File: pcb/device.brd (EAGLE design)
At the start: 160 x 100 mm, 19 parts, among them IC1 TINY13-20PU

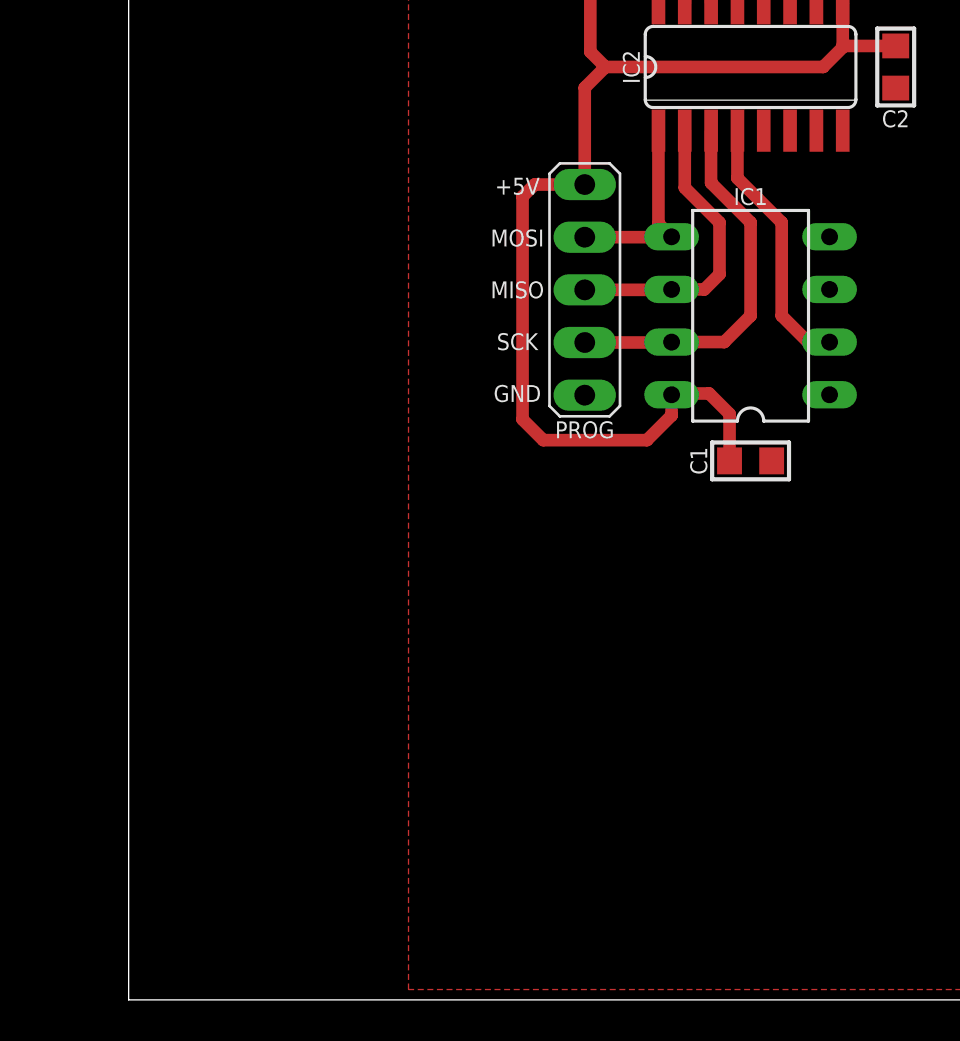
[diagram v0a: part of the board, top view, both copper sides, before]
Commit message: Fix motor connection and add pullup on action pin.
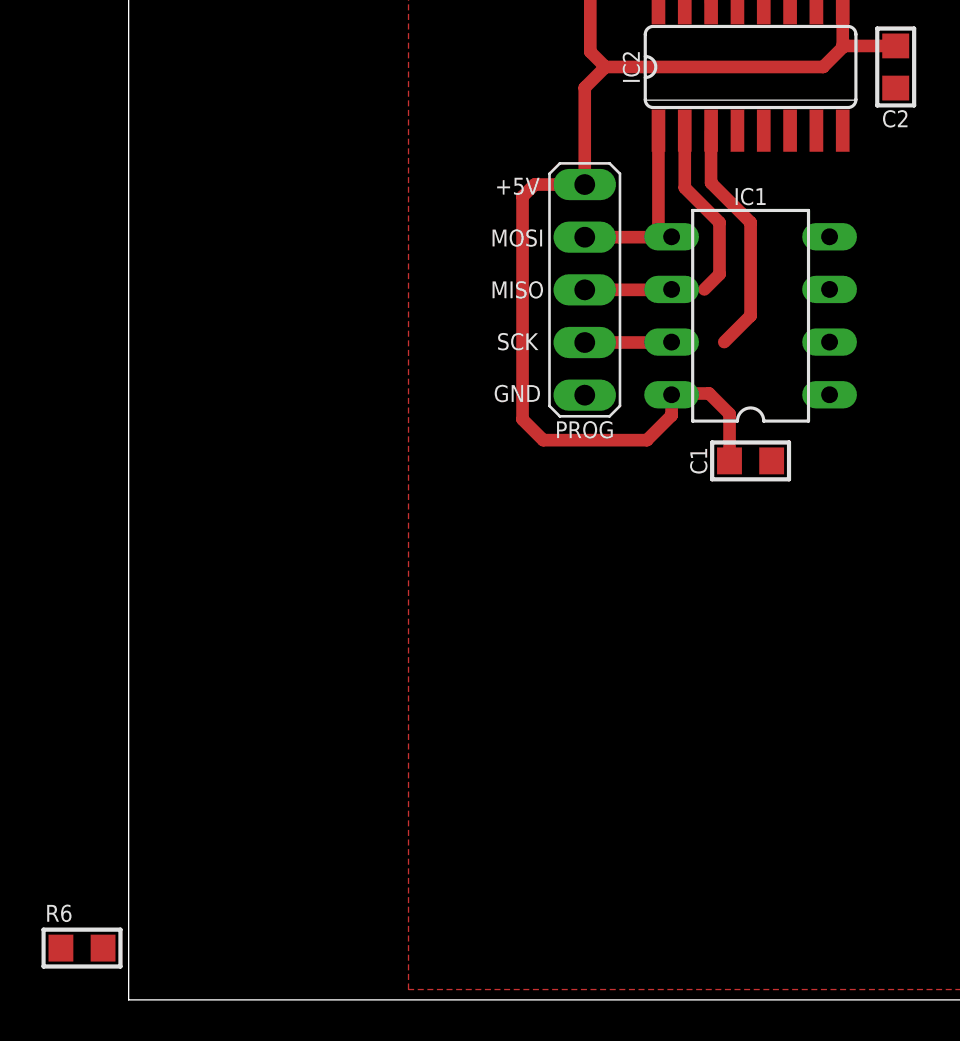
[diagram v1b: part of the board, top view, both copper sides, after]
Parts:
- added R6: 10k, rc-master-smd:R0805
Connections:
- net N$18 renamed !RESET
- removed net N$17: ACTION.1, IC1.3
- new net ROTATE: ACTION.1, IC1.3, R6.1
- net +5V: now also R6.2
- net MISO: now also IC1.7; no longer IC1.6
- net MOSI: now also IC1.6; no longer IC1.5
- net SCK: now also IC1.5; no longer IC1.7
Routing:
- net N$6: track 12.6 -> 0.00 mm
- net SCK: track 18.3 -> 15.7 mm
- net MISO: track 14.4 -> 12.8 mm
- net MOSI: track 9.58 -> 8.65 mm
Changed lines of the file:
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@@
 <attribute name="NAME" x="18.48" y="58.972" size="0.8128" layer="25" font="vector" ratio="18" rot="R90" align="center"/>
 </element>
+<element name="R6" library="rc-master-smd" package="R0805" value="10k" x="-2.25" y="2.5"/>
 </elements>
 <signals>
@@
 <wire x1="22.27" y1="56" x2="22.27" y2="58.746" width="0.6096" layer="1"/>
 <wire x1="22.27" y1="58.746" x2="22.016" y2="59" width="0.6096" layer="1"/>
+<contactref element="R6" pad="2"/>
+<wire x1="-1.234" y1="2.5" x2="20" y2="27" width="0" layer="19" extent="1-1"/>
 </signal>
 <signal name="N$1">
@@
 </signal>
 <signal name="MOSI">
-<contactref element="IC1" pad="5"/>
 <contactref element="IC2" pad="1"/>
 <contactref element="PROG" pad="2"/>
 <wire x1="22" y1="36.79" x2="26.17" y2="36.79" width="0.6096" layer="1"/>
-<wire x1="26.17" y1="36.79" x2="26.19" y2="36.81" width="0.6096" layer="1"/>
 <wire x1="25.555" y1="41.9266" x2="25.555" y2="37.445" width="0.6096" layer="1"/>
-<wire x1="25.555" y1="37.445" x2="26.19" y2="36.81" width="0.6096" layer="1"/>
+<contactref element="IC1" pad="6"/>
+<wire x1="26.17" y1="36.79" x2="25.555" y2="37.445" width="0" layer="19" extent="1-1"/>
+<wire x1="26.19" y1="34.27" x2="26.17" y2="36.79" width="0" layer="19" extent="1-1"/>
 </signal>
 <signal name="MISO">
-<contactref element="IC1" pad="6"/>
 <contactref element="IC2" pad="2"/>
 <contactref element="PROG" pad="3"/>
 <wire x1="22" y1="34.25" x2="26.17" y2="34.25" width="0.6096" layer="1"/>
-<wire x1="26.17" y1="34.25" x2="26.19" y2="34.27" width="0.6096" layer="1"/>
 <wire x1="26.825" y1="41.9266" x2="26.825" y2="39.175" width="0.6096" layer="1"/>
 <wire x1="26.825" y1="39.175" x2="28.5" y2="37.5" width="0.6096" layer="1"/>
-<wire x1="26.19" y1="34.27" x2="27.77" y2="34.27" width="0.6096" layer="1"/>
 <wire x1="27.77" y1="34.27" x2="28.5" y2="35" width="0.6096" layer="1"/>
 <wire x1="28.5" y1="35" x2="28.5" y2="37.5" width="0.6096" layer="1"/>
+<contactref element="IC1" pad="7"/>
+<wire x1="26.17" y1="34.25" x2="27.77" y2="34.27" width="0" layer="19" extent="1-1"/>
+<wire x1="26.19" y1="31.73" x2="26.17" y2="34.25" width="0" layer="19" extent="1-1"/>
 </signal>
 <signal name="SCK">
-<contactref element="IC1" pad="7"/>
 <contactref element="IC2" pad="3"/>
 <contactref element="PROG" pad="4"/>
 <wire x1="28.095" y1="41.9266" x2="28.095" y2="39.405" width="0.6096" layer="1"/>
 <wire x1="28.095" y1="39.405" x2="30" y2="37.5" width="0.6096" layer="1"/>
-<wire x1="26.19" y1="31.73" x2="28.73" y2="31.73" width="0.6096" layer="1"/>
 <wire x1="28.73" y1="31.73" x2="30" y2="33" width="0.6096" layer="1"/>
 <wire x1="30" y1="33" x2="30" y2="37.5" width="0.6096" layer="1"/>
 <wire x1="22" y1="31.71" x2="26.17" y2="31.71" width="0.6096" layer="1"/>
-<wire x1="26.17" y1="31.71" x2="26.19" y2="31.73" width="0.6096" layer="1"/>
-</signal>
-<signal name="N$8">
-<contactref element="IC1" pad="2"/>
-<contactref element="IC2" pad="4"/>
-<wire x1="29.365" y1="41.9266" x2="29.365" y2="39.635" width="0.6096" layer="1"/>
-<wire x1="29.365" y1="39.635" x2="31.5" y2="37.5" width="0.6096" layer="1"/>
-<wire x1="33.81" y1="31.73" x2="32.77" y2="31.73" width="0.6096" layer="1"/>
-<wire x1="32.77" y1="31.73" x2="31.5" y2="33" width="0.6096" layer="1"/>
-<wire x1="31.5" y1="33" x2="31.5" y2="37.5" width="0.6096" layer="1"/>
+<contactref element="IC1" pad="5"/>
+<wire x1="28.095" y1="39.405" x2="26.19" y2="36.81" width="0" layer="19" extent="1-1"/>
+<wire x1="26.17" y1="31.71" x2="28.73" y2="31.73" width="0" layer="19" extent="1-1"/>
 </signal>
 <signal name="BLUE">
@@
 <wire x1="32.54" y1="56" x2="32.54" y2="55.54" width="0.6096" layer="1"/>
 </signal>
-<signal name="N$17">
-<contactref element="IC1" pad="3"/>
-<contactref element="ACTION" pad="1"/>
-<wire x1="43.66" y1="10.79" x2="33.81" y2="34.27" width="0" layer="19" extent="1-1"/>
-</signal>
-<signal name="N$18">
-<contactref element="IC1" pad="1"/>
-<contactref element="MODE" pad="1"/>
-<wire x1="33.81" y1="29.19" x2="43.97" y2="23.96" width="0" layer="19" extent="1-1"/>
-</signal>
 <signal name="N$5">
 <contactref element="R5" pad="1"/>
@@
 <wire x1="19.984" y1="60.966" x2="19.95" y2="61" width="0.6096" layer="1"/>
 </signal>
+<signal name="N$6">
+<contactref element="IC1" pad="2"/>
+<contactref element="IC2" pad="4"/>
+<wire x1="33.81" y1="31.73" x2="29.365" y2="41.9266" width="0" layer="19" extent="1-1"/>
+</signal>
+<signal name="ROTATE">
+<contactref element="IC1" pad="3"/>
+<contactref element="ACTION" pad="1"/>
+<contactref element="R6" pad="1"/>
+<wire x1="43.66" y1="10.79" x2="33.81" y2="34.27" width="0" layer="19" extent="1-1"/>
+<wire x1="-3.266" y1="2.5" x2="43.66" y2="10.79" width="0" layer="19" extent="1-1"/>
+</signal>
+<signal name="!RESET">
+<contactref element="IC1" pad="1"/>
+<contactref element="MODE" pad="1"/>
+<wire x1="33.81" y1="29.19" x2="43.97" y2="23.96" width="0" layer="19" extent="1-1"/>
+</signal>
 </signals>

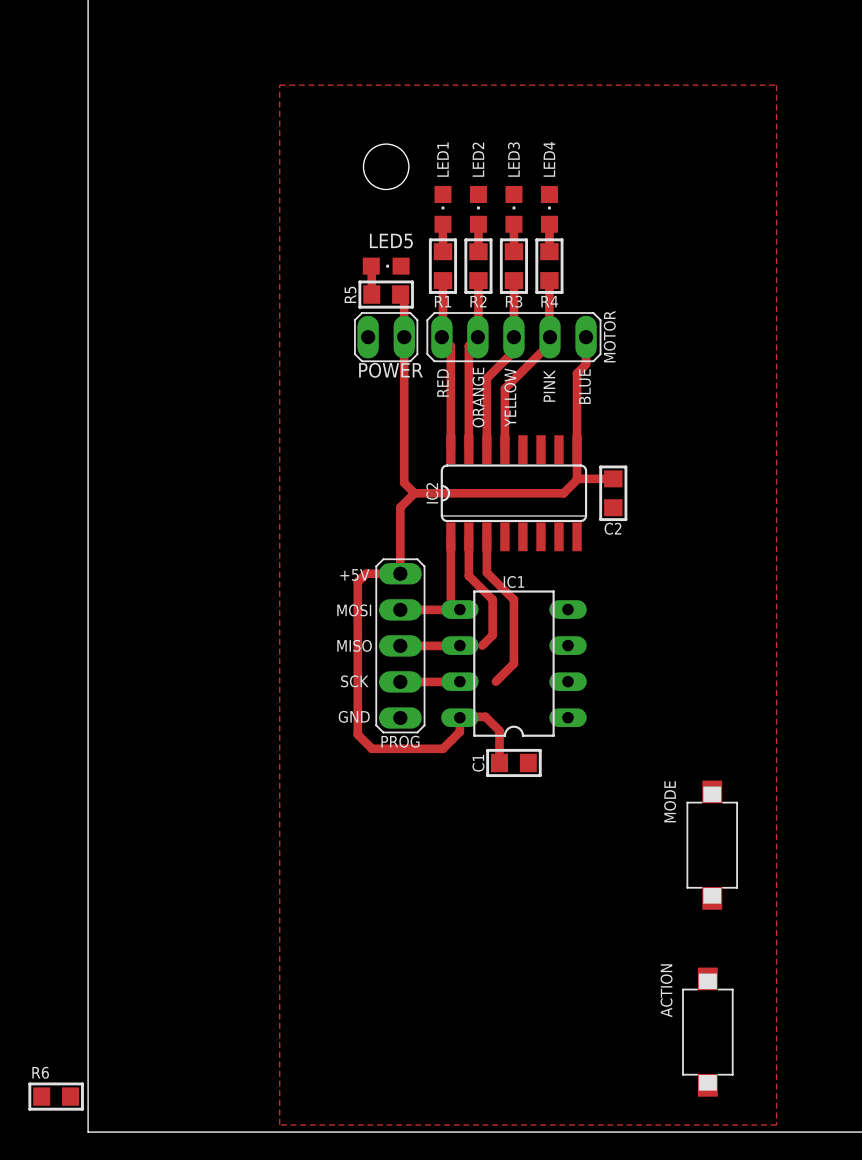
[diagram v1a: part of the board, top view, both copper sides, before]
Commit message: Almost ready PCB.
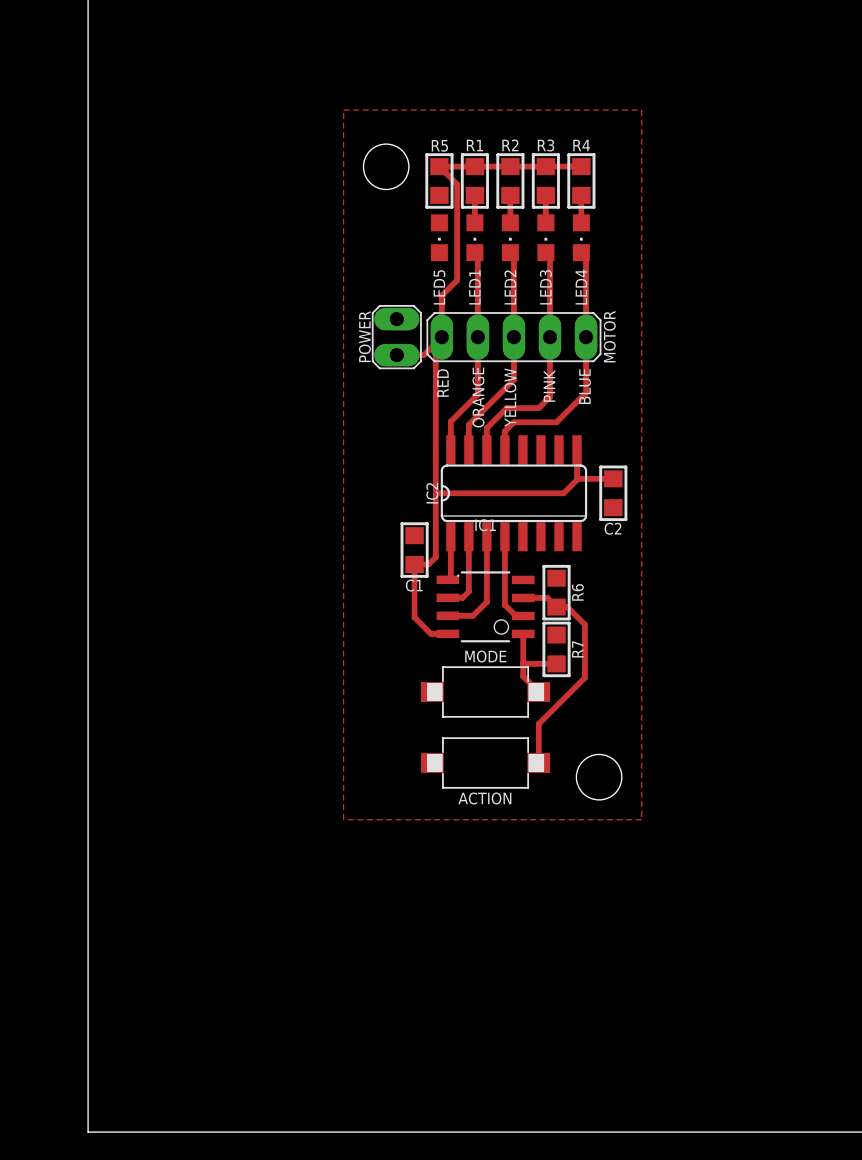
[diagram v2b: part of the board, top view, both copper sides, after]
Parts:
- removed PROG: (no value), pinhead-fixdrills:1X05
- added R7: 10k, rc-master-smd:R0805
- IC1: value TINY13-20PU -> TINY13-20SSU; device avr:DIL08 -> avr:8S1
- moved R6 50.0 mm to (33.0, 38.0), turned to 90 degrees
- moved ACTION 24.6 mm to (28.0, 26.0), turned to 180 degrees
- moved MODE 19.3 mm to (28.0, 31.0), turned to 180 degrees
- moved C1 16.6 mm to (23.0, 41.0), turned to 90 degrees
- moved R5 8.84 mm to (24.8, 67.0), turned to 90 degrees
- moved R1 6.41 mm to (27.2, 67.0), turned to 90 degrees
- moved R2 6.41 mm to (29.8, 67.0), turned to 90 degrees
- moved R3 6.41 mm to (32.2, 67.0), turned to 90 degrees
- moved R4 6.41 mm to (34.8, 67.0), turned to 90 degrees
- moved IC1 4.47 mm to (28.0, 37.0)
- moved LED5 4.25 mm to (24.8, 63.0), turned to 180 degrees
- moved LED1 3.01 mm to (27.2, 63.0), turned to 180 degrees
- moved LED2 3.01 mm to (29.8, 63.0), turned to 180 degrees
- moved LED3 3.01 mm to (32.2, 63.0), turned to 180 degrees
- moved LED4 3.01 mm to (34.8, 63.0), turned to 180 degrees
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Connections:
- removed net MISO: IC1.7, IC2.2, PROG.3
- removed net MOSI: IC1.6, IC2.1, PROG.2
- removed net SCK: IC1.5, IC2.3, PROG.4
- new net N$6: IC1.5, IC2.1
- new net N$7: IC1.6, IC2.2
- new net N$8: IC1.7, IC2.3
- net !RESET: now also R7.1
- net +5V: now also MOTOR.1, R1.2, R2.2, R3.2, R4.2, R7.2; no longer MOTOR.5, PROG.1
- net BLUE: now also IC2.13, LED4.C, MOTOR.5; no longer IC2.16, MOTOR.1, R1.2
- net GND: no longer LED1.C, LED2.C, LED3.C, LED4.C, PROG.5
- net ORANGE: now also IC2.16, LED1.C, MOTOR.2; no longer IC2.13, MOTOR.4, R4.2
- net PINK: now also IC2.14, LED3.C, MOTOR.4; no longer IC2.15, MOTOR.2, R2.2
- net YELLOW: now also IC2.15, LED2.C; no longer IC2.14, R3.2
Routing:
- net ROTATE: track 0.00 -> 16.2 mm
- net SCK: track 15.7 -> 0.00 mm
- net MISO: track 12.8 -> 0.00 mm
- net MOSI: track 8.65 -> 0.00 mm
- net +5V: track 73.8 -> 65.6 mm
- net N$8: track 0.00 -> 7.74 mm
- net !RESET: track 0.00 -> 6.90 mm
- net N$9: track 0.00 -> 6.40 mm
- net BLUE: track 12.2 -> 18.1 mm
- net N$7: track 0.00 -> 5.51 mm
- net PINK: track 12.2 -> 17.2 mm
- net N$6: track 0.00 -> 3.11 mm
- net YELLOW: track 12.7 -> 15.3 mm
- net N$5: track 2.01 -> 0.00 mm
- net ORANGE: track 13.2 -> 14.8 mm
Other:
- board text removed: "+5V"
- board text removed: "GND"
- board text removed: "MISO"
- board text removed: "MOSI"
- board text removed: "SCK"
